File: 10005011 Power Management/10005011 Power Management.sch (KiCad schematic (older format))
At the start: 0 parts

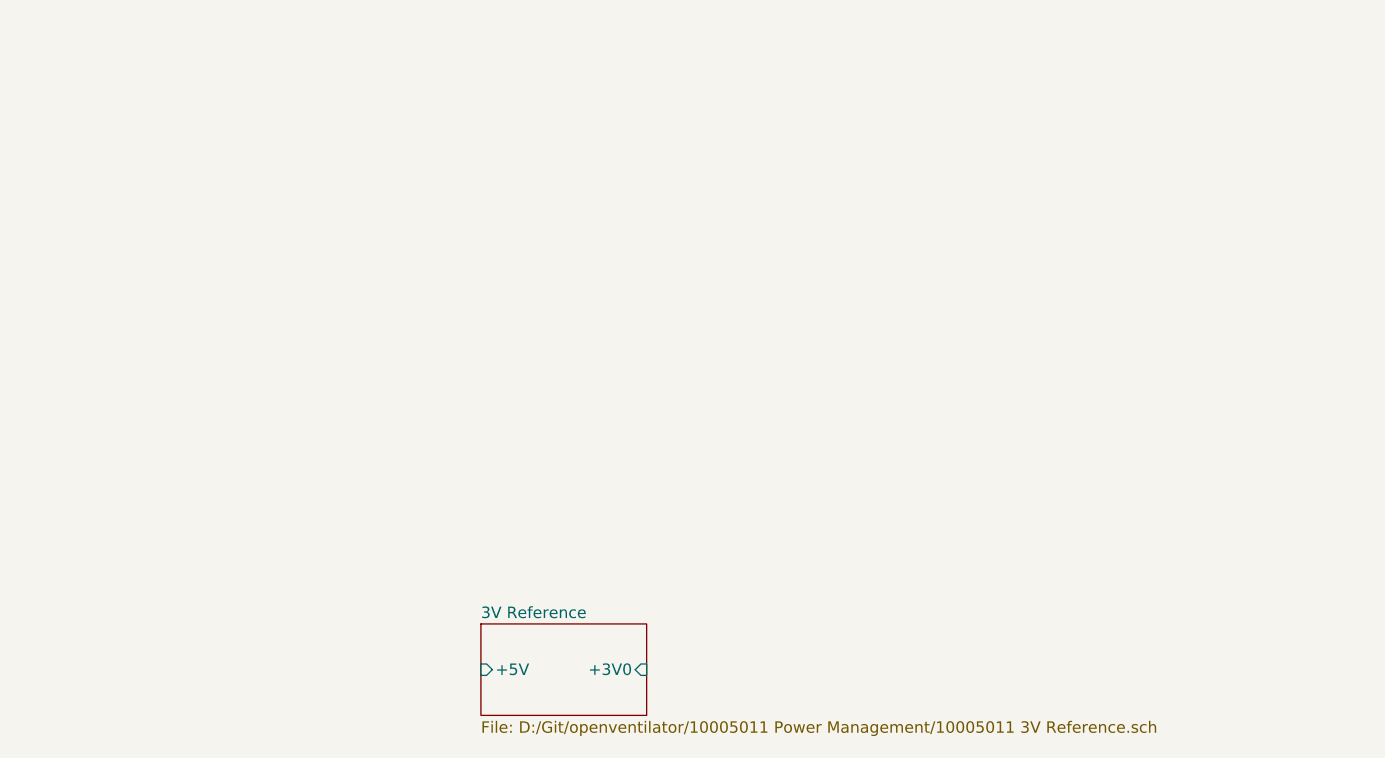
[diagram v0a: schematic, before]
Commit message: added power flags to library and PIC to schematic
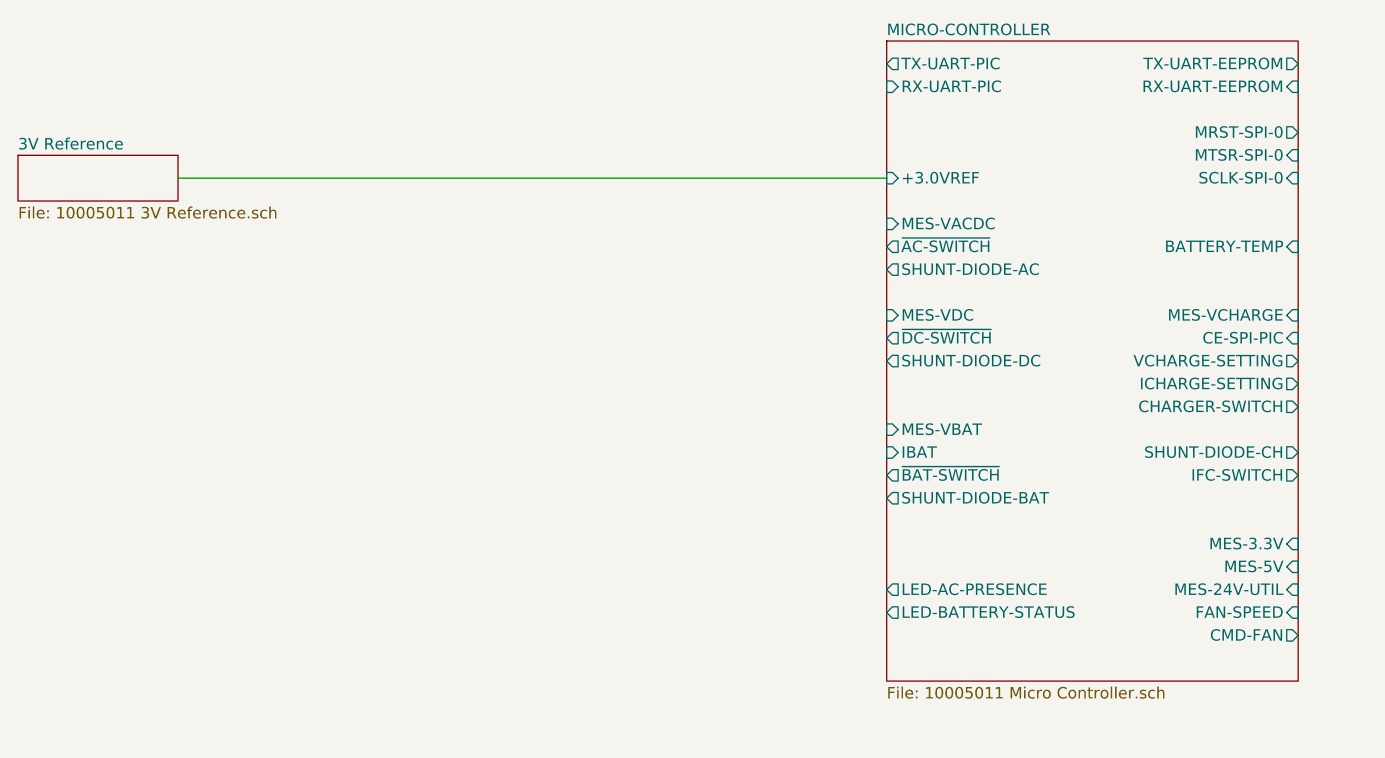
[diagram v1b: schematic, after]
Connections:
- wire segments 0 -> 1
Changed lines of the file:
@@
-EESchema Schematic File Version 5
-EELAYER 33 0
+EESchema Schematic File Version 4
+LIBS:10005011 Power Management-cache
+EELAYER 26 0
 EELAYER END
 $Descr USLetter 11000 8500
 encoding utf-8
-Sheet 1 2
+Sheet 1 3
 Title ""
 Date ""
@@
 Comment3 ""
 Comment4 ""
-Comment5 ""
-Comment6 ""
-Comment7 ""
-Comment8 ""
-Comment9 ""
 $EndDescr
 $Sheet
-S 2625 4650 725  400
+S 600  2600 700  200
 U 5E88D608
 F0 "3V Reference" 50
-F1 "D:/Git/openventilator/10005011 Power Management/10005011 3V Reference.sch" 50
-F2 "+3V0" I R 3350 4850 50
-F3 "+5V" I L 2625 4850 50
+F1 "10005011 3V Reference.sch" 50
 $EndSheet
+$Sheet
+S 4400 2100 1800 2800
+U 5E8E2802
+F0 "MICRO-CONTROLLER" 50
+F1 "10005011 Micro Controller.sch" 50
+F2 "~AC-SWITCH" O L 4400 3000 50
+F3 "SHUNT-DIODE-AC" O L 4400 3100 50
+F4 "~DC-SWITCH" O L 4400 3400 50
+F5 "SHUNT-DIODE-DC" O L 4400 3500 50
+F6 "TX-UART-EEPROM" O R 6200 2200 50
+F7 "RX-UART-EEPROM" I R 6200 2300 50
+F8 "MRST-SPI-0" O R 6200 2500 50
+F9 "MTSR-SPI-0" I R 6200 2600 50
+F10 "SCLK-SPI-0" I R 6200 2700 50
+F11 "FAN-SPEED" I R 6200 4600 50
+F12 "LED-AC-PRESENCE" O L 4400 4500 50
+F13 "LED-BATTERY-STATUS" O L 4400 4600 50
+F14 "TX-UART-PIC" O L 4400 2200 50
+F15 "RX-UART-PIC" I L 4400 2300 50
+F16 "VCHARGE-SETTING" O R 6200 3500 50
+F17 "ICHARGE-SETTING" O R 6200 3600 50
+F18 "CE-SPI-PIC" I R 6200 3400 50
+F19 "MES-VBAT" I L 4400 3800 50
+F20 "MES-5V" I R 6200 4400 50
+F21 "MES-24V-UTIL" I R 6200 4500 50
+F22 "~BAT-SWITCH" O L 4400 4000 50
+F23 "SHUNT-DIODE-BAT" O L 4400 4100 50
+F24 "CHARGER-SWITCH" O R 6200 3700 50
+F25 "IFC-SWITCH" O R 6200 4000 50
+F26 "SHUNT-DIODE-CH" O R 6200 3900 50
+F27 "CMD-FAN" O R 6200 4700 50
+F28 "MES-VDC" I L 4400 3300 50
+F29 "MES-VACDC" I L 4400 2900 50
+F30 "+3.0VREF" I L 4400 2700 50
+F31 "MES-VCHARGE" I R 6200 3300 50
+F32 "IBAT" I L 4400 3900 50
+F33 "BATTERY-TEMP" I R 6200 3000 50
+F34 "MES-3.3V" I R 6200 4300 50
+$EndSheet
+Wire Wire Line
+	1300 2700 4400 2700
 $EndSCHEMATC

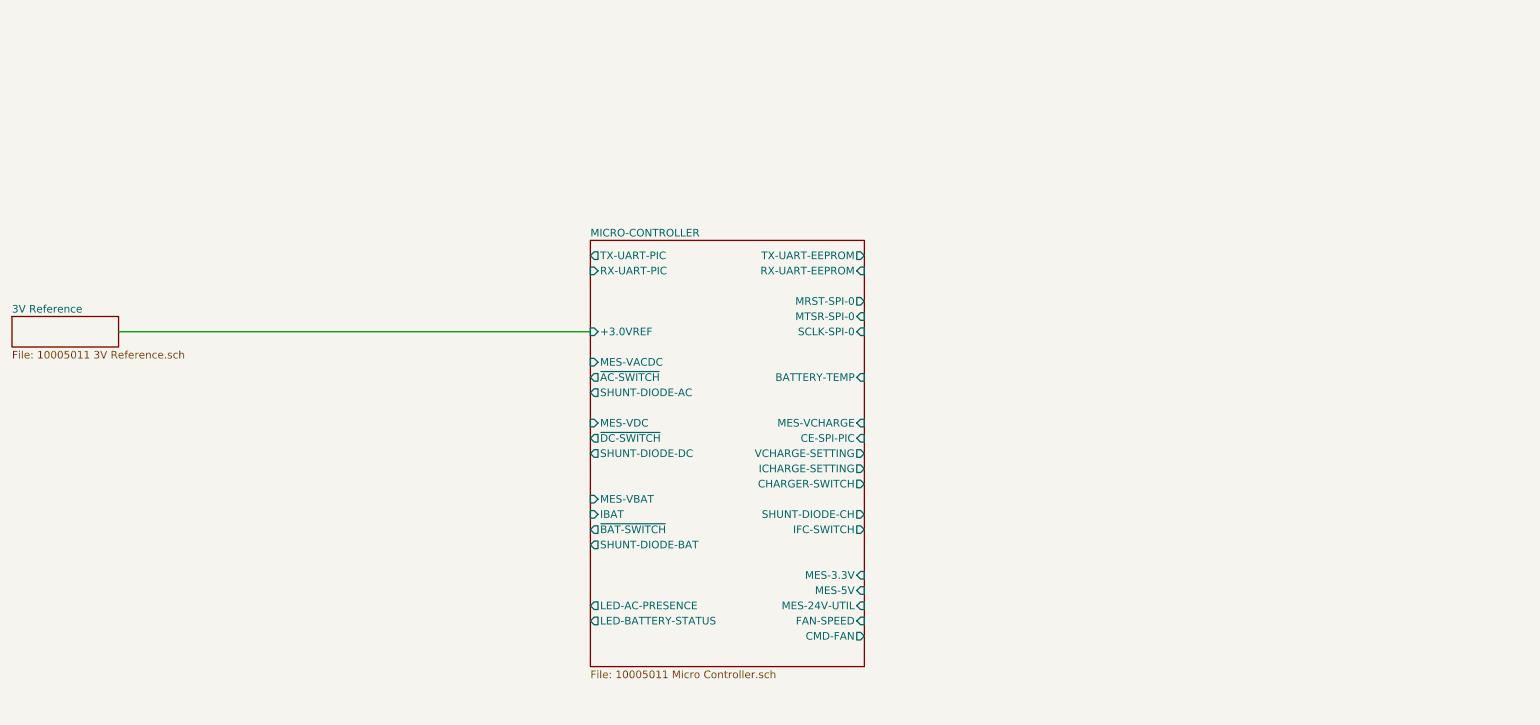
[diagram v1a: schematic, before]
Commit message: added UART schematics from pages 1 and 3
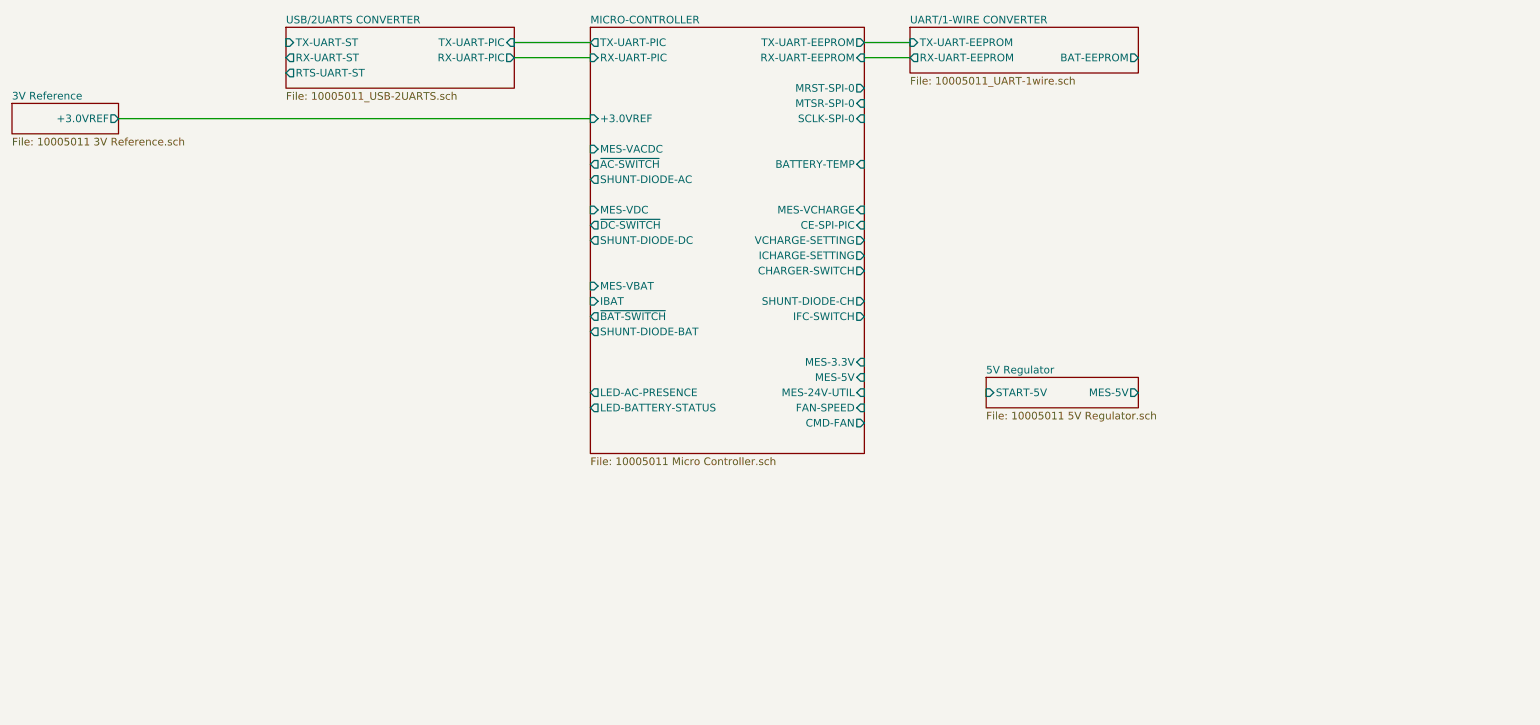
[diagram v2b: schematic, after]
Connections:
- wire segments 1 -> 5
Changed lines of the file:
@@
 EESchema Schematic File Version 4
-LIBS:10005011 Power Management-cache
-EELAYER 26 0
+EELAYER 30 0
 EELAYER END
 $Descr USLetter 11000 8500
 encoding utf-8
-Sheet 1 3
+Sheet 1 6
 Title ""
 Date ""
@@
 $EndDescr
 $Sheet
-S 600  2600 700  200
+S 600  1200 700  200
 U 5E88D608
 F0 "3V Reference" 50
 F1 "10005011 3V Reference.sch" 50
+F2 "+3.0VREF" O R 1300 1300 50
 $EndSheet
 $Sheet
-S 4400 2100 1800 2800
+S 4400 700  1800 2800
 U 5E8E2802
 F0 "MICRO-CONTROLLER" 50
 F1 "10005011 Micro Controller.sch" 50
-F2 "~AC-SWITCH" O L 4400 3000 50
-F3 "SHUNT-DIODE-AC" O L 4400 3100 50
-F4 "~DC-SWITCH" O L 4400 3400 50
-F5 "SHUNT-DIODE-DC" O L 4400 3500 50
-F6 "TX-UART-EEPROM" O R 6200 2200 50
-F7 "RX-UART-EEPROM" I R 6200 2300 50
-F8 "MRST-SPI-0" O R 6200 2500 50
-F9 "MTSR-SPI-0" I R 6200 2600 50
-F10 "SCLK-SPI-0" I R 6200 2700 50
-F11 "FAN-SPEED" I R 6200 4600 50
-F12 "LED-AC-PRESENCE" O L 4400 4500 50
-F13 "LED-BATTERY-STATUS" O L 4400 4600 50
-F14 "TX-UART-PIC" O L 4400 2200 50
-F15 "RX-UART-PIC" I L 4400 2300 50
-F16 "VCHARGE-SETTING" O R 6200 3500 50
-F17 "ICHARGE-SETTING" O R 6200 3600 50
-F18 "CE-SPI-PIC" I R 6200 3400 50
-F19 "MES-VBAT" I L 4400 3800 50
-F20 "MES-5V" I R 6200 4400 50
-F21 "MES-24V-UTIL" I R 6200 4500 50
-F22 "~BAT-SWITCH" O L 4400 4000 50
-F23 "SHUNT-DIODE-BAT" O L 4400 4100 50
-F24 "CHARGER-SWITCH" O R 6200 3700 50
-F25 "IFC-SWITCH" O R 6200 4000 50
-F26 "SHUNT-DIODE-CH" O R 6200 3900 50
-F27 "CMD-FAN" O R 6200 4700 50
-F28 "MES-VDC" I L 4400 3300 50
-F29 "MES-VACDC" I L 4400 2900 50
-F30 "+3.0VREF" I L 4400 2700 50
-F31 "MES-VCHARGE" I R 6200 3300 50
-F32 "IBAT" I L 4400 3900 50
-F33 "BATTERY-TEMP" I R 6200 3000 50
-F34 "MES-3.3V" I R 6200 4300 50
+F2 "~AC-SWITCH" O L 4400 1600 50
+F3 "SHUNT-DIODE-AC" O L 4400 1700 50
+F4 "~DC-SWITCH" O L 4400 2000 50
+F5 "SHUNT-DIODE-DC" O L 4400 2100 50
+F6 "TX-UART-EEPROM" O R 6200 800 50
+F7 "RX-UART-EEPROM" I R 6200 900 50
+F8 "MRST-SPI-0" O R 6200 1100 50
+F9 "MTSR-SPI-0" I R 6200 1200 50
+F10 "SCLK-SPI-0" I R 6200 1300 50
+F11 "FAN-SPEED" I R 6200 3200 50
+F12 "LED-AC-PRESENCE" O L 4400 3100 50
+F13 "LED-BATTERY-STATUS" O L 4400 3200 50
+F14 "TX-UART-PIC" O L 4400 800 50
+F15 "RX-UART-PIC" I L 4400 900 50
+F16 "VCHARGE-SETTING" O R 6200 2100 50
+F17 "ICHARGE-SETTING" O R 6200 2200 50
+F18 "CE-SPI-PIC" I R 6200 2000 50
+F19 "MES-VBAT" I L 4400 2400 50
+F20 "MES-5V" I R 6200 3000 50
+F21 "MES-24V-UTIL" I R 6200 3100 50
+F22 "~BAT-SWITCH" O L 4400 2600 50
+F23 "SHUNT-DIODE-BAT" O L 4400 2700 50
+F24 "CHARGER-SWITCH" O R 6200 2300 50
+F25 "IFC-SWITCH" O R 6200 2600 50
+F26 "SHUNT-DIODE-CH" O R 6200 2500 50
+F27 "CMD-FAN" O R 6200 3300 50
+F28 "MES-VDC" I L 4400 1900 50
+F29 "MES-VACDC" I L 4400 1500 50
+F30 "+3.0VREF" I L 4400 1300 50
+F31 "MES-VCHARGE" I R 6200 1900 50
+F32 "IBAT" I L 4400 2500 50
+F33 "BATTERY-TEMP" I R 6200 1600 50
+F34 "MES-3.3V" I R 6200 2900 50
 $EndSheet
 Wire Wire Line
-	1300 2700 4400 2700
+	1300 1300 4400 1300
+$Sheet
+S 7000 3000 1000 200
+U 5E8F17C0
+F0 "5V Regulator" 50
+F1 "10005011 5V Regulator.sch" 50
+F2 "START-5V" I L 7000 3100 50
+F3 "MES-5V" O R 8000 3100 50
+$EndSheet
+$Sheet
+S 6500 700  1500 300
+U 5E91E4AA
+F0 "UART/1-WIRE CONVERTER" 50
+F1 "10005011_UART-1wire.sch" 50
+F2 "BAT-EEPROM" O R 8000 900 50
+F3 "RX-UART-EEPROM" O L 6500 900 50
+F4 "TX-UART-EEPROM" I L 6500 800 50
+$EndSheet
+Wire Wire Line
+	6200 800  6500 800
+Wire Wire Line
+	6200 900  6500 900
+$Sheet
+S 2400 700  1500 400
+U 5E937D30
+F0 "USB/2UARTS CONVERTER" 50
+F1 "10005011_USB-2UARTS.sch" 50
+F2 "RX-UART-PIC" O R 3900 900 50
+F3 "RX-UART-ST" O L 2400 900 50
+F4 "RTS-UART-ST" O L 2400 1000 50
+F5 "TX-UART-ST" I L 2400 800 50
+F6 "TX-UART-PIC" I R 3900 800 50
+$EndSheet
+Wire Wire Line
+	3900 800  4400 800
+Wire Wire Line
+	3900 900  4400 900
 $EndSCHEMATC

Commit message: update ALIM1 as virtual component and pin arrangement according to footprint, PST9 adn PST14 updated refdes
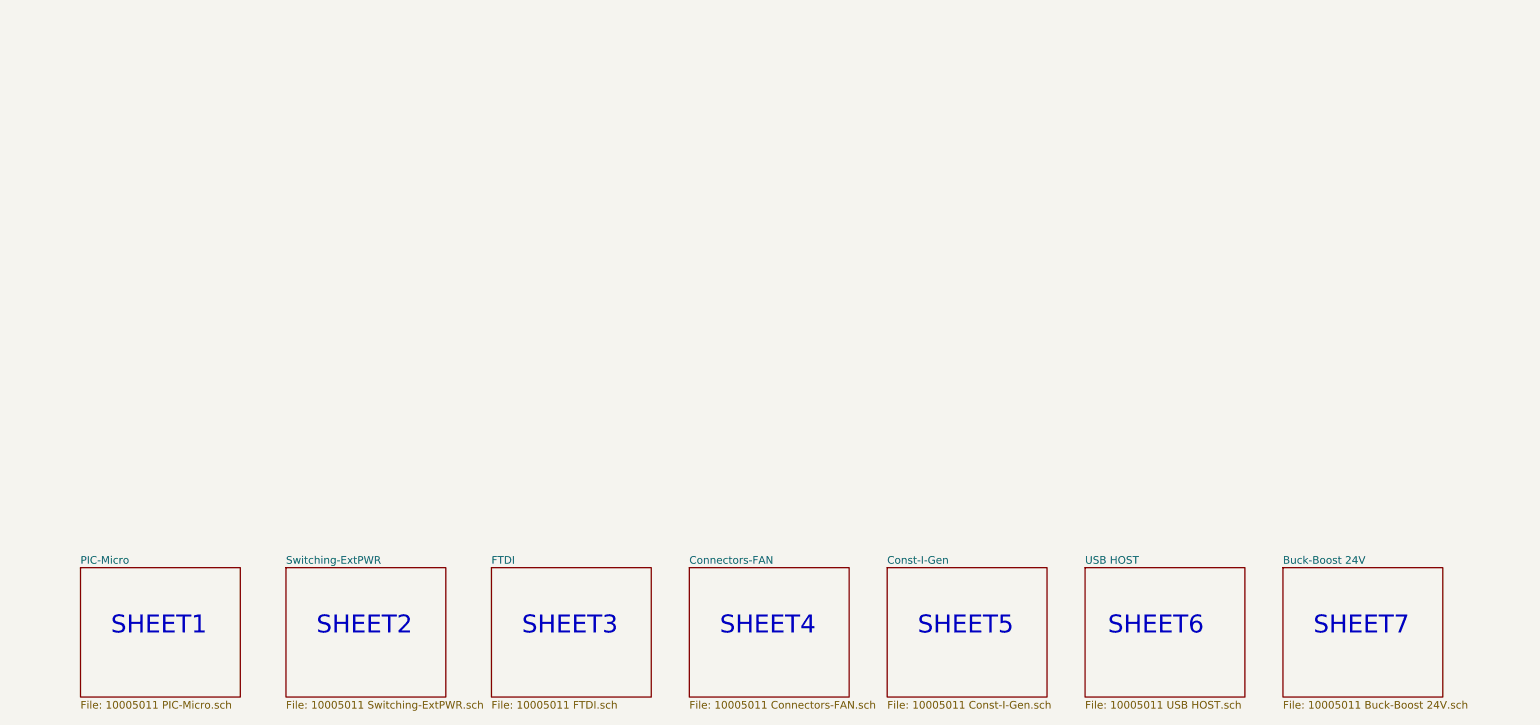
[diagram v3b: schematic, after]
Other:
- note added: "SHEET1"
- note added: "SHEET2"
- note added: "SHEET3"
- note added: "SHEET4"
- note added: "SHEET5"
- note added: "SHEET6"
- note added: "SHEET7"
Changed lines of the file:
@@
 $Descr USLetter 11000 8500
 encoding utf-8
-Sheet 1 6
+Sheet 1 8
 Title ""
 Date ""
@@
 $EndDescr
 $Sheet
-S 600  1200 700  200
-U 5E88D608
-F0 "3V Reference" 50
-F1 "10005011 3V Reference.sch" 50
-F2 "+3.0VREF" O R 1300 1300 50
+S 8950 4250 1050 850
+U 5E92767C
+F0 "Buck-Boost 24V" 50
+F1 "10005011 Buck-Boost 24V.sch" 50
 $EndSheet
 $Sheet
-S 4400 700  1800 2800
-U 5E8E2802
-F0 "MICRO-CONTROLLER" 50
-F1 "10005011 Micro Controller.sch" 50
-F2 "~AC-SWITCH" O L 4400 1600 50
-F3 "SHUNT-DIODE-AC" O L 4400 1700 50
-F4 "~DC-SWITCH" O L 4400 2000 50
-F5 "SHUNT-DIODE-DC" O L 4400 2100 50
-F6 "TX-UART-EEPROM" O R 6200 800 50
-F7 "RX-UART-EEPROM" I R 6200 900 50
-F8 "MRST-SPI-0" O R 6200 1100 50
-F9 "MTSR-SPI-0" I R 6200 1200 50
-F10 "SCLK-SPI-0" I R 6200 1300 50
-F11 "FAN-SPEED" I R 6200 3200 50
-F12 "LED-AC-PRESENCE" O L 4400 3100 50
-F13 "LED-BATTERY-STATUS" O L 4400 3200 50
-F14 "TX-UART-PIC" O L 4400 800 50
-F15 "RX-UART-PIC" I L 4400 900 50
-F16 "VCHARGE-SETTING" O R 6200 2100 50
-F17 "ICHARGE-SETTING" O R 6200 2200 50
-F18 "CE-SPI-PIC" I R 6200 2000 50
-F19 "MES-VBAT" I L 4400 2400 50
-F20 "MES-5V" I R 6200 3000 50
-F21 "MES-24V-UTIL" I R 6200 3100 50
-F22 "~BAT-SWITCH" O L 4400 2600 50
-F23 "SHUNT-DIODE-BAT" O L 4400 2700 50
-F24 "CHARGER-SWITCH" O R 6200 2300 50
-F25 "IFC-SWITCH" O R 6200 2600 50
-F26 "SHUNT-DIODE-CH" O R 6200 2500 50
-F27 "CMD-FAN" O R 6200 3300 50
-F28 "MES-VDC" I L 4400 1900 50
-F29 "MES-VACDC" I L 4400 1500 50
-F30 "+3.0VREF" I L 4400 1300 50
-F31 "MES-VCHARGE" I R 6200 1900 50
-F32 "IBAT" I L 4400 2500 50
-F33 "BATTERY-TEMP" I R 6200 1600 50
-F34 "MES-3.3V" I R 6200 2900 50
+S 7650 4250 1050 850
+U 5E9C3EF6
+F0 "USB HOST" 50
+F1 "10005011 USB HOST.sch" 50
 $EndSheet
-Wire Wire Line
-	1300 1300 4400 1300
+Text Notes 9150 4700 0    118  ~ 0
+SHEET7
+Text Notes 7800 4700 0    118  ~ 0
+SHEET6
 $Sheet
-S 7000 3000 1000 200
-U 5E8F17C0
-F0 "5V Regulator" 50
-F1 "10005011 5V Regulator.sch" 50
-F2 "START-5V" I L 7000 3100 50
-F3 "MES-5V" O R 8000 3100 50
+S 5050 4250 1050 850
+U 5FB0520C
+F0 "Connectors-FAN" 50
+F1 "10005011 Connectors-FAN.sch" 50
 $EndSheet
+Text Notes 5250 4700 0    118  ~ 0
+SHEET4
 $Sheet
-S 6500 700  1500 300
-U 5E91E4AA
-F0 "UART/1-WIRE CONVERTER" 50
-F1 "10005011_UART-1wire.sch" 50
-F2 "BAT-EEPROM" O R 8000 900 50
-F3 "RX-UART-EEPROM" O L 6500 900 50
-F4 "TX-UART-EEPROM" I L 6500 800 50
+S 3750 4250 1050 850
+U 5FDBA600
+F0 "FTDI" 50
+F1 "10005011 FTDI.sch" 50
 $EndSheet
-Wire Wire Line
-	6200 800  6500 800
-Wire Wire Line
-	6200 900  6500 900
+Text Notes 3950 4700 0    118  ~ 0
+SHEET3
 $Sheet
-S 2400 700  1500 400
-U 5E937D30
-F0 "USB/2UARTS CONVERTER" 50
-F1 "10005011_USB-2UARTS.sch" 50
-F2 "RX-UART-PIC" O R 3900 900 50
-F3 "RX-UART-ST" O L 2400 900 50
-F4 "RTS-UART-ST" O L 2400 1000 50
-F5 "TX-UART-ST" I L 2400 800 50
-F6 "TX-UART-PIC" I R 3900 800 50
+S 6350 4250 1050 850
+U 5FEC1BCD
+F0 "Const-I-Gen" 50
+F1 "10005011 Const-I-Gen.sch" 50
 $EndSheet
-Wire Wire Line
-	3900 800  4400 800
-Wire Wire Line
-	3900 900  4400 900
+Text Notes 6550 4700 0    118  ~ 0
+SHEET5
+$Sheet
+S 2400 4250 1050 850
+U 5FEC5422
+F0 "Switching-ExtPWR" 50
+F1 "10005011 Switching-ExtPWR.sch" 50
+$EndSheet
+Text Notes 2600 4700 0    118  ~ 0
+SHEET2
+$Sheet
+S 1050 4250 1050 850
+U 5FEC80F9
+F0 "PIC-Micro" 50
+F1 "10005011 PIC-Micro.sch" 50
+$EndSheet
+Text Notes 1250 4700 0    118  ~ 0
+SHEET1
 $EndSCHEMATC
